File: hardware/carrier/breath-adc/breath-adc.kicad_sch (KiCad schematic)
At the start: 6 parts

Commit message: Main board: apply the chosen parts to every symbol and row
Every main-board and adapter symbol now carries Footprint, Manufacturer,
MPN, LCSC and Assembly. The values come from the selections whose
datasheets are banked. The BOM rows follow those choices:

- D-USBOR is the SS14 (SMA).
- J-LED is four solder pads, not a connector.
- L-BUCK-IN is 22 uH, C-BUCK-IN is a UCM electrolytic, C-STRIP-BULK is
  470 uF 25 V.
- D-TVS-BREATH is the PESD12VS1UA (SOD-323); the UB is SOD523.
- J-UMB is the hanxia header. Its posts go through the adapter and its
  tails through the tongue; the old wording had them swapped.
- U-BUCK and U-BREATH say where to buy.
- C-ADC-BULK is 1206 if fitted.

The body and geometry follow the chosen parts:

- The J-UMB and J-MCU envelopes in config/body.yaml are now read off the
  parts' drawings.
- J-MCU is longer, so the regulator block moved and the right-hand ribbon
  header followed it by 1.5 mm. The RH key board is re-laid out, with C8
  moving with the header's 3V3 pin. It checks clean.
- A mount candidate is now nudged by up to 3 mm before it is dropped. All
  seven main-board mounts hold.

New footprints and pages:

- New woody.pretty footprints: the MPXV4006DP (case 1351-01) from
  breath-sense-link.md's land pattern, and the NE8FAV from Neutrik's
  layout, mirrored to the top view.
- The input-LC derivation uses the chosen capacitor's banked ESR: Q is at
  most 1.8, and the margin is 120x worst case.
- The main-board README lists what is still open before layout.

Co-Authored-By: Claude Opus 5.5 <noreply@anthropic.com>
Claude-Session: https://claude.ai/code/session_01LmB4muFXnoLprWX4JzuJ5A
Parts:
- C-AA-ADC: footprint (none) -> Capacitor_SMD:C_0805_2012Metric; Assembly (none) -> machine; LCSC (none) -> C22402129; MPN (none) -> C0805C473J3GACTU; Manufacturer (none) -> KEMET
- C-ADC-BULK: footprint (none) -> Capacitor_SMD:C_1206_3216Metric; Assembly (none) -> machine; LCSC (none) -> C89632; MPN (none) -> CL31B106KBHNNNE; Manufacturer (none) -> Samsung Electro-Mechanics
- C-DEC-ADC: footprint (none) -> Capacitor_SMD:C_0805_2012Metric; Assembly (none) -> machine; LCSC (none) -> C49678; MPN (none) -> CC0805KRX7R9BB104; Manufacturer (none) -> YAGEO
- R-ADCDIV-L: footprint (none) -> Resistor_SMD:R_0805_2012Metric; Assembly (none) -> machine; LCSC (none) -> C869203; MPN (none) -> RT0805FRE0715KL; Manufacturer (none) -> YAGEO
- R-ADCDIV-U: footprint (none) -> Resistor_SMD:R_0805_2012Metric; Assembly (none) -> machine; LCSC (none) -> C869153; MPN (none) -> RT0805FRE0710KL; Manufacturer (none) -> YAGEO
- U-ADC: footprint (none) -> Package_SO:SOIC-8_3.9x4.9mm_P1.27mm; Assembly (none) -> machine; LCSC (none) -> C56997; MPN (none) -> MCP3202-CI/SN; Manufacturer (none) -> Microchip
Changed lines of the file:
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@@
     (property "Reference" "R-ADCDIV-U" (at 43.18 49.53 0) (effects (font (size 1.27 1.27)) (justify left)))
     (property "Value" "10k 1%" (at 43.18 52.07 0) (effects (font (size 1.27 1.27)) (justify left)))
-    (property "Footprint" "" (at 39.37 50.8 0) (effects (font (size 1.27 1.27)) hide))
+    (property "Footprint" "Resistor_SMD:R_0805_2012Metric" (at 39.37 50.8 0) (effects (font (size 1.27 1.27)) hide))
     (property "Datasheet" "" (at 40.64 50.8 0) (effects (font (size 1.27 1.27)) hide))
     (property "Row" "R-ADCDIV-U" (at 40.64 50.8 0) (effects (font (size 1.27 1.27)) hide))
     (property "Pins" "1=1 2=2" (at 40.64 50.8 0) (effects (font (size 1.27 1.27)) hide))
     (property "Note" "UPPER LEG, AND >=10k IS A SPEC RATHER THAN A VALUE: below that, 5V-before-3V3 sequencing pushes about 2.5 mA into the ADC's ESD clamp on every power-up. DIVIDE AFTER THE BUFFER, never before" (at 40.64 50.8 0) (effects (font (size 1.27 1.27)) hide))
+    (property "Manufacturer" "YAGEO" (at 40.64 50.8 0) (effects (font (size 1.27 1.27)) hide))
+    (property "MPN" "RT0805FRE0710KL" (at 40.64 50.8 0) (effects (font (size 1.27 1.27)) hide))
+    (property "LCSC" "C869153" (at 40.64 50.8 0) (effects (font (size 1.27 1.27)) hide))
+    (property "Assembly" "machine" (at 40.64 50.8 0) (effects (font (size 1.27 1.27)) hide))
     (pin "1")
     (pin "2")
@@
     (property "Reference" "R-ADCDIV-L" (at 93.98 49.53 0) (effects (font (size 1.27 1.27)) (justify left)))
     (property "Value" "15k 1%" (at 93.98 52.07 0) (effects (font (size 1.27 1.27)) (justify left)))
-    (property "Footprint" "" (at 90.17 50.8 0) (effects (font (size 1.27 1.27)) hide))
+    (property "Footprint" "Resistor_SMD:R_0805_2012Metric" (at 90.17 50.8 0) (effects (font (size 1.27 1.27)) hide))
     (property "Datasheet" "" (at 91.44 50.8 0) (effects (font (size 1.27 1.27)) hide))
     (property "Row" "R-ADCDIV-L" (at 91.44 50.8 0) (effects (font (size 1.27 1.27)) hide))
     (property "Pins" "1=1 2=2" (at 91.44 50.8 0) (effects (font (size 1.27 1.27)) hide))
     (property "Note" "Lower leg, to the analog star. 15k against 10k is the 0.6x that lands the sensor's full scale inside a 3V3 ADC" (at 91.44 50.8 0) (effects (font (size 1.27 1.27)) hide))
+    (property "Manufacturer" "YAGEO" (at 91.44 50.8 0) (effects (font (size 1.27 1.27)) hide))
+    (property "MPN" "RT0805FRE0715KL" (at 91.44 50.8 0) (effects (font (size 1.27 1.27)) hide))
+    (property "LCSC" "C869203" (at 91.44 50.8 0) (effects (font (size 1.27 1.27)) hide))
+    (property "Assembly" "machine" (at 91.44 50.8 0) (effects (font (size 1.27 1.27)) hide))
     (pin "1")
     (pin "2")
@@
     (property "Reference" "C-AA-ADC" (at 144.78 49.53 0) (effects (font (size 1.27 1.27)) (justify left)))
     (property "Value" "47nF C0G/NP0" (at 144.78 52.07 0) (effects (font (size 1.27 1.27)) (justify left)))
-    (property "Footprint" "" (at 143.51 54.61 0) (effects (font (size 1.27 1.27)) hide))
+    (property "Footprint" "Capacitor_SMD:C_0805_2012Metric" (at 143.51 54.61 0) (effects (font (size 1.27 1.27)) hide))
     (property "Datasheet" "" (at 142.24 50.8 0) (effects (font (size 1.27 1.27)) hide))
     (property "Row" "C-AA-ADC" (at 142.24 50.8 0) (effects (font (size 1.27 1.27)) hide))
     (property "Pins" "1=1 2=2" (at 142.24 50.8 0) (effects (font (size 1.27 1.27)) hide))
     (property "Note" "Anti-alias at the divider node. It has to settle inside the sample window, which is what stops the upper leg going higher still" (at 142.24 50.8 0) (effects (font (size 1.27 1.27)) hide))
+    (property "Manufacturer" "KEMET" (at 142.24 50.8 0) (effects (font (size 1.27 1.27)) hide))
+    (property "MPN" "C0805C473J3GACTU" (at 142.24 50.8 0) (effects (font (size 1.27 1.27)) hide))
+    (property "LCSC" "C22402129" (at 142.24 50.8 0) (effects (font (size 1.27 1.27)) hide))
+    (property "Assembly" "machine" (at 142.24 50.8 0) (effects (font (size 1.27 1.27)) hide))
     (pin "1")
     (pin "2")
@@
     (property "Reference" "U-ADC" (at 34.29 95.25 0) (effects (font (size 1.27 1.27))))
     (property "Value" "MCP3202-CI/SN" (at 52.07 95.25 0) (effects (font (size 1.27 1.27))))
-    (property "Footprint" "" (at 40.64 109.22 0) (effects (font (size 1.27 1.27)) hide))
+    (property "Footprint" "Package_SO:SOIC-8_3.9x4.9mm_P1.27mm" (at 40.64 109.22 0) (effects (font (size 1.27 1.27)) hide))
     (property "Datasheet" "" (at 40.64 101.6 0) (effects (font (size 1.27 1.27)) hide))
     (property "Row" "U-ADC" (at 40.64 106.68 0) (effects (font (size 1.27 1.27)) hide))
@@
     (property "Note" "NO VREF PIN - VDD IS THE REFERENCE, and that reference is the dev board's LDO, the same rail the 24 key pull-ups load. CH1 is spare" (at 40.64 106.68 0) (effects (font (size 1.27 1.27)) hide))
     (property "Pins_source" "datasheets/analog/MCP3202-CI-SN.pdf p.1 Package Types (SOIC) and Table 3-1" (at 40.64 106.68 0) (effects (font (size 1.27 1.27)) hide))
+    (property "Manufacturer" "Microchip" (at 40.64 106.68 0) (effects (font (size 1.27 1.27)) hide))
+    (property "MPN" "MCP3202-CI/SN" (at 40.64 106.68 0) (effects (font (size 1.27 1.27)) hide))
+    (property "LCSC" "C56997" (at 40.64 106.68 0) (effects (font (size 1.27 1.27)) hide))
+    (property "Assembly" "machine" (at 40.64 106.68 0) (effects (font (size 1.27 1.27)) hide))
     (pin "1")
     (pin "2")
@@
     (property "Reference" "C-ADC-BULK" (at 43.18 186.69 0) (effects (font (size 1.27 1.27)) (justify left)))
     (property "Value" "10uF" (at 43.18 189.23 0) (effects (font (size 1.27 1.27)) (justify left)))
-    (property "Footprint" "" (at 41.91 191.77 0) (effects (font (size 1.27 1.27)) hide))
+    (property "Footprint" "Capacitor_SMD:C_1206_3216Metric" (at 41.91 191.77 0) (effects (font (size 1.27 1.27)) hide))
     (property "Datasheet" "" (at 40.64 187.96 0) (effects (font (size 1.27 1.27)) hide))
     (property "Row" "C-ADC-BULK" (at 40.64 187.96 0) (effects (font (size 1.27 1.27)) hide))
     (property "Pins" "1=1 2=2" (at 40.64 187.96 0) (effects (font (size 1.27 1.27)) hide))
     (property "Note" "Local reservoir on the reference rail" (at 40.64 187.96 0) (effects (font (size 1.27 1.27)) hide))
+    (property "Manufacturer" "Samsung Electro-Mechanics" (at 40.64 187.96 0) (effects (font (size 1.27 1.27)) hide))
+    (property "MPN" "CL31B106KBHNNNE" (at 40.64 187.96 0) (effects (font (size 1.27 1.27)) hide))
+    (property "LCSC" "C89632" (at 40.64 187.96 0) (effects (font (size 1.27 1.27)) hide))
+    (property "Assembly" "machine" (at 40.64 187.96 0) (effects (font (size 1.27 1.27)) hide))
     (pin "1")
     (pin "2")
@@
     (property "Reference" "C-DEC-ADC" (at 93.98 186.69 0) (effects (font (size 1.27 1.27)) (justify left)))
     (property "Value" "100nF" (at 93.98 189.23 0) (effects (font (size 1.27 1.27)) (justify left)))
-    (property "Footprint" "" (at 92.71 191.77 0) (effects (font (size 1.27 1.27)) hide))
+    (property "Footprint" "Capacitor_SMD:C_0805_2012Metric" (at 92.71 191.77 0) (effects (font (size 1.27 1.27)) hide))
     (property "Datasheet" "" (at 91.44 187.96 0) (effects (font (size 1.27 1.27)) hide))
     (property "Row" "C-DECOUPLE-CARRIER" (at 91.44 187.96 0) (effects (font (size 1.27 1.27)) hide))
     (property "Pins" "1=1 2=2" (at 91.44 187.96 0) (effects (font (size 1.27 1.27)) hide))
+    (property "Manufacturer" "YAGEO" (at 91.44 187.96 0) (effects (font (size 1.27 1.27)) hide))
+    (property "MPN" "CC0805KRX7R9BB104" (at 91.44 187.96 0) (effects (font (size 1.27 1.27)) hide))
+    (property "LCSC" "C49678" (at 91.44 187.96 0) (effects (font (size 1.27 1.27)) hide))
+    (property "Assembly" "machine" (at 91.44 187.96 0) (effects (font (size 1.27 1.27)) hide))
     (pin "1")
     (pin "2")

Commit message: Breath ADC and reference: C-ADC-BULK fitted, no series R on C-REF-OUT, ADC provenance from DS21034F
C-ADC-BULK fitted as the reference pin's reservoir; the PWM question it was
proposed for is not what it can filter, so E9's scope test is specified on
the page. C-REF-OUT takes no series resistor (SBOS410O 9.4.1.1: optional;
noise peaking stays >100x below an LSB). The MCP3202's clamp-current claim
now cites the datasheet, which rates no injection current at all.

Co-Authored-By: Claude Opus 5.5 <noreply@anthropic.com>
Claude-Session: https://claude.ai/code/session_01LmB4muFXnoLprWX4JzuJ5A
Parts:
- C-ADC-BULK: Note Local reservoir on the reference rail -> Reservoir on the reference rail, at U-ADC pin 8 beside C-DE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
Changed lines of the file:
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@@
     (property "Row" "C-ADC-BULK" (at 40.64 187.96 0) (effects (font (size 1.27 1.27)) hide))
     (property "Pins" "1=1 2=2" (at 40.64 187.96 0) (effects (font (size 1.27 1.27)) hide))
-    (property "Note" "Local reservoir on the reference rail" (at 40.64 187.96 0) (effects (font (size 1.27 1.27)) hide))
+    (property "Note" "Reservoir on the reference rail, at U-ADC pin 8 beside C-DEC-ADC. Fitted; it does not filter LED PWM (E9 tests that)" (at 40.64 187.96 0) (effects (font (size 1.27 1.27)) hide))
     (property "Manufacturer" "Samsung Electro-Mechanics" (at 40.64 187.96 0) (effects (font (size 1.27 1.27)) hide))
     (property "MPN" "CL31B106KBHNNNE" (at 40.64 187.96 0) (effects (font (size 1.27 1.27)) hide))

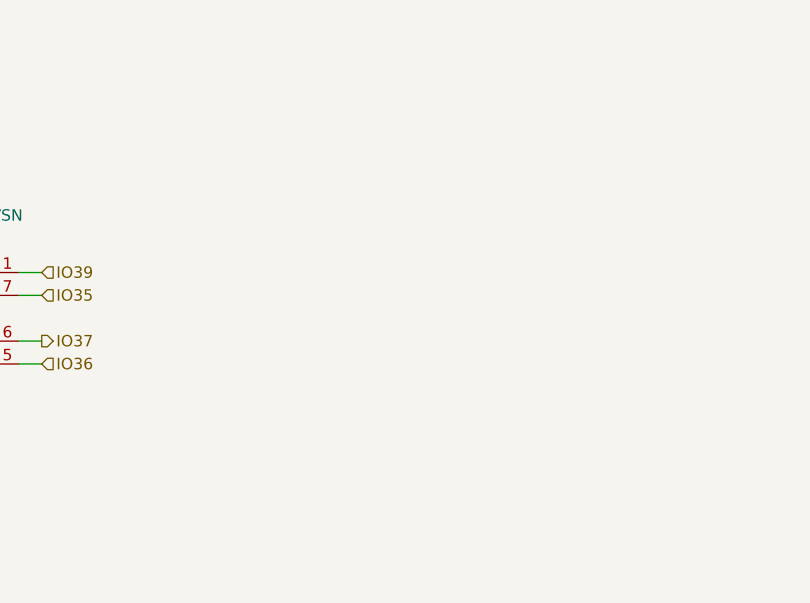
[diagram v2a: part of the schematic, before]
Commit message: #11 F5, F2: CS_ADC pulled up (R45); E9 measures the converter's ripple; the 55 dB is ADC_IN's
#11 F5 (verified, partly): IO39 is MTCK, whose reset pull-up depends on
EFUSE_DIS_PAD_JTAG (ESP32-S3 datasheet p.17-18, note 7: 0 = WPU, 1 =
floating). So CS_ADC is not floating by default, but it is with that fuse
burned. R-CS-PULL-ADC (10k, the R-CS-PULL-INST part) on the breath-adc
sheet, main-board R45, from IO39 to DEV_3V3 beside U-ADC pin 1. New BOM
row in the breath-adc fragment; page interface table, component table and a
paragraph; sheet and main board re-exported and rendered; breath-adc,
breath-output-stage and the MPXV7007 fallback sims re-run on the new
netlist (hash only, no number moved).

#11 F2 (doc half; the filter itself is an owner decision with #14 A1 and
#12-3): the "Simulated" paragraph's "55 dB at the buck's rate" now says
ADC_IN's own path; C-AA-ADC's BOM note says the same and loses its history
(rule 2b); E9 gains the LEDs-off, full-scale-blow measurement of VDD at
pin 8, which the off-vs-sweeping comparison cannot see.

Gate-Red: tree known-red - main-board .kicad_pcb awaits re-layout (R45 not on it yet), photos/clash stale, breath-adc vdd-ripple fails pending the owner's filter decision

Co-Authored-By: Claude Opus 5.5 <noreply@anthropic.com>
Claude-Session: https://claude.ai/code/session_01LmB4muFXnoLprWX4JzuJ5A
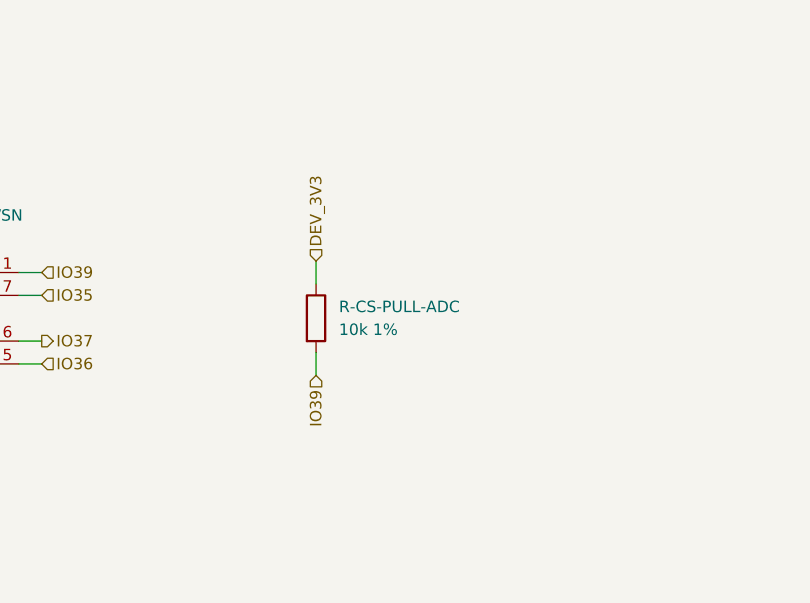
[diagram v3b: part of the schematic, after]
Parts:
- added R-CS-PULL-ADC: 10k 1%, Resistor_SMD:R_0805_2012Metric, symbol Device:R
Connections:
- net DEV_3V3: now also R-CS-PULL-ADC.1
- net IO39: now also R-CS-PULL-ADC.2
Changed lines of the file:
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@@
   (no_connect (at 27.94 111.76))
   (text "FROM THE HAND-WRITTEN NETLIST THIS SHEET REPLACES (verbatim; the part notes are on each part's Note field):\n\nAUTHORITATIVE for connectivity. THE DRAWING IS ON ANOTHER PAGE - carrier.md §2 draws the whole breath path in\none picture. This circuit is the divider and the MCP3202 at the end of it.\n\nSpare input, unconnected by decision - the Interfaces table says so." (at 256.54 38.099999999999994 0) (effects (font (size 1.27 1.27)) (justify left top)))
+  (symbol (lib_id "Device:R") (at 91.44 106.68 0) (unit 1)
+    (in_bom yes) (on_board yes) (dnp no)
+    (property "Reference" "R-CS-PULL-ADC" (at 93.98 105.41 0) (effects (font (size 1.27 1.27)) (justify left)))
+    (property "Value" "10k 1%" (at 93.98 107.95 0) (effects (font (size 1.27 1.27)) (justify left)))
+    (property "Footprint" "Resistor_SMD:R_0805_2012Metric" (at 91.44 106.68 0) (effects (font (size 1.27 1.27)) hide))
+    (property "Datasheet" "" (at 91.44 106.68 0) (effects (font (size 1.27 1.27)) hide))
+    (property "Row" "R-CS-PULL-ADC" (at 91.44 106.68 0) (effects (font (size 1.27 1.27)) hide))
+    (property "Pins" "1=1 2=2" (at 91.44 106.68 0) (effects (font (size 1.27 1.27)) hide))
+    (property "Note" "CS_ADC's idle pull-up (#11 F5): IO39 to DEV_3V3, beside U-ADC pin 1. IO39 is MTCK, whose weak pull-up at reset depends on an eFuse - 'IE 7', note 7: EFUSE_DIS_PAD_JTAG 0, WPU enabled; 1, pin floating [ds ESP32-S3-datasheet-v2.2.pdf p.17-18] - and ESP-IDF burns that fuse when secure boot is built for release [from memory]. This holds U-ADC deselected from reset until the firmware drives the pin whatever the fuses say, as R-CS-PULL-INST holds CS_MOD on the same shared host. IO39 is not a strapping pin (GPIO0/3/45/46, p.26)" (at 91.44 106.68 0) (effects (font (size 1.27 1.27)) hide))
+    (property "Pins_source" "a two-terminal resistor" (at 91.44 106.68 0) (effects (font (size 1.27 1.27)) hide))
+    (property "Manufacturer" "UNI-ROYAL(Uniroyal Elec)" (at 91.44 106.68 0) (effects (font (size 1.27 1.27)) hide))
+    (property "MPN" "0805W8F1002T5E" (at 91.44 106.68 0) (effects (font (size 1.27 1.27)) hide))
+    (property "LCSC" "C17414" (at 91.44 106.68 0) (effects (font (size 1.27 1.27)) hide))
+    (property "Assembly" "machine" (at 91.44 106.68 0) (effects (font (size 1.27 1.27)) hide))
+    (pin "1")
+    (pin "2")
+    (instances (project "main-board" (path "/b12a49ac-ffa0-5078-b2ba-e15d161f1936/0cf3bab1-830b-5708-931a-4147821b88e1" (reference "R45") (unit 1))) (project "breath-adc" (path "/c79f4df5-783d-57a4-af84-ebef797ab12e" (reference "R-CS-PULL-ADC") (unit 1))))
+  )
+  (wire (pts (xy 91.44 102.87) (xy 91.44 100.33)) (stroke (width 0) (type default)))
+  (hierarchical_label "DEV_3V3" (shape input) (at 91.44 100.33 90) (effects (font (size 1.27 1.27)) (justify left))
+    (property "Dir" "in" (at 91.44 100.33 0) (effects (font (size 1.27 1.27)) hide))
+    (property "From" "carrier/carrier" (at 91.44 100.33 0) (effects (font (size 1.27 1.27)) hide)))
+  (wire (pts (xy 91.44 110.49) (xy 91.44 113.03)) (stroke (width 0) (type default)))
+  (hierarchical_label "IO39" (shape input) (at 91.44 113.03 270) (effects (font (size 1.27 1.27)) (justify right))
+    (property "Dir" "in" (at 91.44 113.03 0) (effects (font (size 1.27 1.27)) hide))
+    (property "From" "carrier/carrier" (at 91.44 113.03 0) (effects (font (size 1.27 1.27)) hide)))
   (sheet_instances (path "/" (page "1")))
 )

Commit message: Owner decisions D1, D2, D3, D5, CMRR: the parts on the sheets (#11, #14, #15, #16, #5, #12)
The owner's choices of 2026-10-03 (working chat), applied to the KiCad sheets,
exported, rendered, and carried into the BOM fragments:

- D1 (#11 F2, #14 A1, #12-3), "10 ohm + 22 uF + 10 uF": breath-adc gains
  R-ADC-VDD (10R 1% 0805, UNI-ROYAL 0805W8F100JT5E, C17415, JLC basic) from
  DEV_3V3 to a new local net ADC_VDD = U-ADC pin 8, with C-ADC-VDD (22 uF
  X5R 25 V 1206, Samsung CL31A226KAHNNNE, C12891, JLC basic) beside the
  existing C-ADC-BULK and C-DEC-ADC (C3 kept); a PWR_FLAG on ADC_VDD for
  ERC. power-entry-instrument gains C-BUCK-OUT (10 uF X5R 50 V 1206,
  Samsung CL31A106KBHNNNE, C13585, JLC basic) at U-BUCK-A's OUT (main-board
  U5, the R-78E5.0 - RECOM's standard application, #14 A1 item 3).
  Main board: R47, C42, C43.
- D5: U-ADC CH1 tied to AGND_INST.
- D2 (#15 C2, #16 B2), "Yes, all 4 channels": a second SP0504BAHTG at J5
  on CHAIN_SCK, CHAIN_SHLD, HOP_LT_RH, HOP_RH_RT - main-board U11 on the
  root sheet, U-TVS-CHAIN-RH on the key-chain-loom sheet; row qty 2.
- D3 (#15 C3): R-SPI-SER (R1-R3) Panasonic ERJ-P08F82R0V (C4065013, 0 at
  JLC and LCSC; in-stock equivalent Vishay CRCW120682R0FKEAHP, C1854869,
  named in the row); R-SER-BREATH-INST (R38/R39) ERJ-P08F1001V (C4261071,
  JLC 4,299).
- CMRR (#5-5), "Tighten cap matching": C-CM-BREATH a matched pair, each
  within 0.5 % of the pair's mean, from one reel of the 1 % C0G, measured
  and hand-fitted (no 1.5 nF C0G is catalogued tighter than 1 %).

Banked: Samsung CL31A226KAHNNNE and CL31A106KBHNNNE spec sheets, Vishay
CRCW-HP e3 (fragment .manifest-R51-owner-decisions.csv). Also two module
sims the deff676 merge staled and these changes do not touch (panel-led,
digital-and-supervision) re-run: 0 failed.

Gate-Red: sims staled by these netlists are re-running in the next commits; main-board .kicad_pcb awaits wave-3 placement of R47, C42, C43, U11 (and fab/ renders); known stale photos/clash

Co-Authored-By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
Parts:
- added C-ADC-VDD: 22uF, Capacitor_SMD:C_1206_3216Metric, symbol Device:C
- added R-ADC-VDD: 10R 1%, Resistor_SMD:R_0805_2012Metric, symbol Device:R
- C-ADC-BULK: Note Reservoir on the reference rail, at U-ADC pin 8 beside C-DE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 -> On ADC_VDD, the reference rail, at U-ADC pin 8 beside C-DEC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
- U-ADC: Note NO VREF PIN - VDD IS THE REFERENCE, and that reference is the dev board's LDO, the same rail the 24 key pull-ups load. CH1 is spare -> NO VREF PIN - VDD IS THE REFERENCE, and that reference is the dev board's LDO, fed through R-ADC-VDD from the dev board's LDO, the rail the key pull-ups load. CH1 is tied to AGND_INST (owner, 2026-10-03, D5): a known zero for a self-test, and no floating input beside CH0
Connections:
- net AGND_INST: now also U-ADC.3 (CH1), C-ADC-VDD.2
- net DEV_3V3: now also R-ADC-VDD.1; no longer C-ADC-BULK.1, C-DEC-ADC.1, U-ADC.8 (VDD/VREF)
- new net ADC_VDD: C-ADC-BULK.1, C-ADC-VDD.1, C-DEC-ADC.1, R-ADC-VDD.2, U-ADC.8 (VDD/VREF)
- no-connect marks 1 -> 0
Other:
- note added: "FROM THE HAND-WRITTEN NETLIST THIS SHEET REPLACES (verbatim; the part notes are on each part's Note field): AUTHORITATIVE for connectivity. THE DRAWING IS ON ANOTHER PAGE - carrier.md §2 draws the whole breath path in one picture. This circuit is the divider and the MCP3202 at the end of it. CH1 is tied to AGND_INST (owner, 2026-10-03, D5). U-ADC's VDD = VREF is ADC_VDD, filtered from DEV_3V3 by 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"
- note removed: "FROM THE HAND-WRITTEN NETLIST THIS SHEET REPLACES (verbatim; the part notes are on each part's Note field): AUTHORITATIVE for connectivity. THE DRAWING IS ON ANOTHER PAGE - carrier.md §2 draws the whole breath path in one picture. This circuit is the divider and the MCP3202 at the end of it. Spare input, unconnected by decision - the Interfaces table says so."
